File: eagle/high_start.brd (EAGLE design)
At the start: 100.8 x 80.8 mm, 34 parts, among them IC1 7805TV, Q1 16Mhz, Q2 IRF510, Q3 IRF510, Q4 IRF510, U2 ATMEGA328P_PDIP

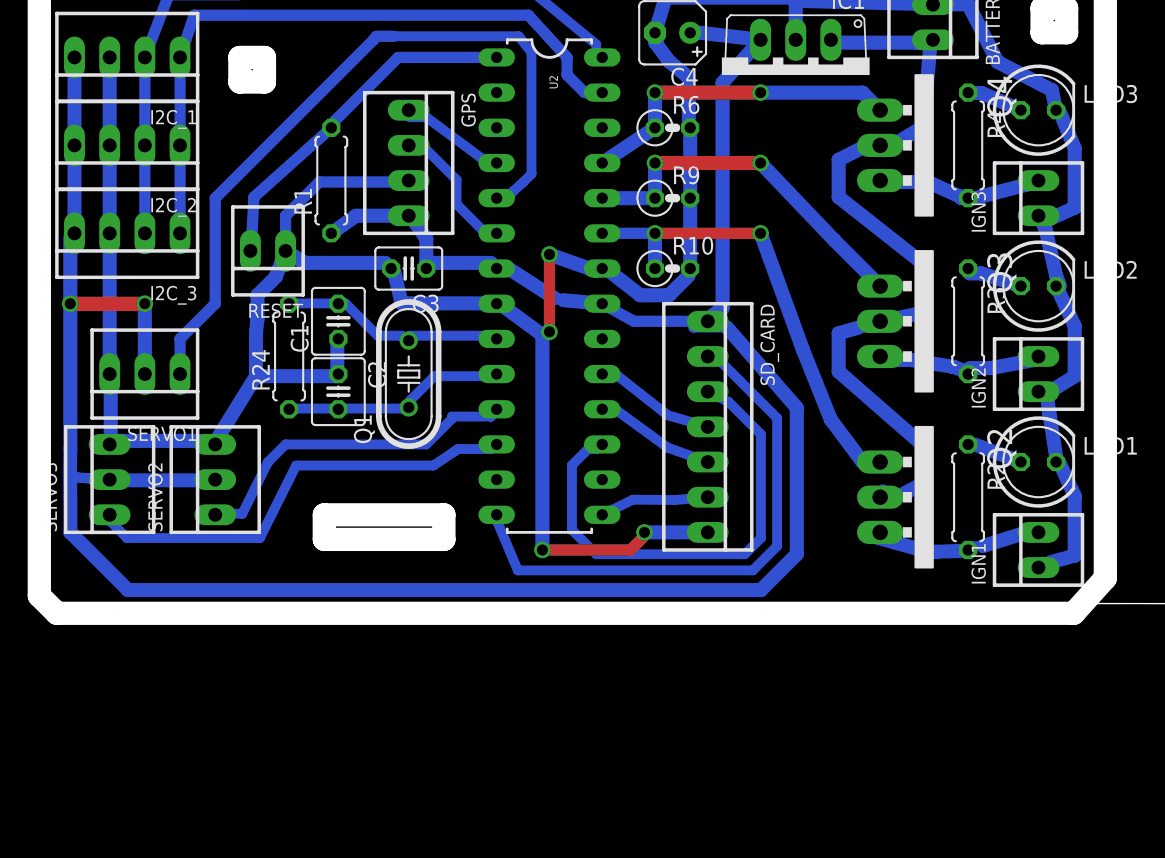
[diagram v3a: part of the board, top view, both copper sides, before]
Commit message: moved igniter FETs to low side
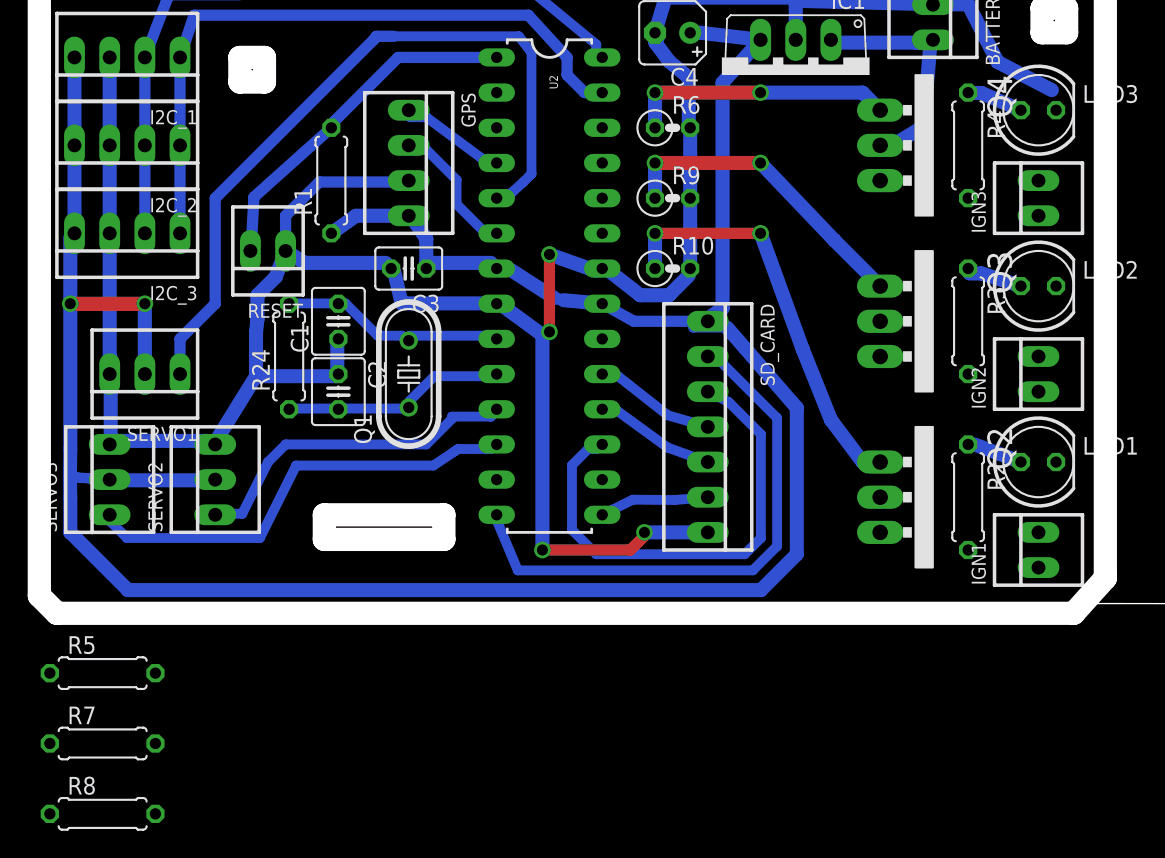
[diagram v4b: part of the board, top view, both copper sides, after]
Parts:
- added R5, R7, R8: 220, rcl:0207/7
- R2, R3, R4: value 330 -> 1k
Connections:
- new net N$12: IGN1.1, Q2.2, R2.2
- new net N$13: IGN2.1, Q3.2, R3.2
- new net N$14: IGN3.1, Q4.2, R4.2
- net +9V: now also IGN1.2, IGN2.2, IGN3.2; no longer Q2.2, Q3.2, Q4.2
- net GND: now also Q2.3, Q3.3, Q4.3; no longer IGN1.1, IGN2.1, IGN3.1
- net N$18: now also R5.2; no longer U2.23
- net N$19: now also R8.2; no longer U2.24
- net N$20: now also R7.2; no longer U2.25
- net N$24: now also R5.1, U2.23; no longer IGN1.2, Q2.3, R2.2
- net N$25: now also R7.1, U2.25; no longer IGN2.2, Q3.3, R3.2
- net N$26: now also R8.1, U2.24; no longer IGN3.2, Q4.3, R4.2
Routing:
- net GND: track 239.5 -> 197.1 mm
- net +9V: track 59.4 -> 18.0 mm
- net N$24: track 12.9 -> 0.00 mm
- net N$25: track 12.3 -> 0.00 mm
- net N$26: track 12.1 -> 0.00 mm
- net N$20: track 23.9 -> 19.3 mm
- net N$18: track 33.4 -> 29.6 mm
- net N$19: track 26.4 -> 22.6 mm

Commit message: janky rerouted
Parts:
- R10, R6, R9: device rcl:0207/2V -> rcl:0207/7
- moved R7 63.8 mm to (48.3, 35.6)
- moved R8 63.8 mm to (48.3, 30.5)
- moved R5 53.9 mm to (48.3, 25.4)
- moved R10 5.48 mm to (50.3, 22.9), turned to 180 degrees
- moved R9 5.48 mm to (50.3, 27.9), turned to 180 degrees
- moved R6 5.48 mm to (50.3, 33.0), turned to 180 degrees
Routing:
- net GND: track 197.1 -> 299.4 mm
- net +9V: track 18.0 -> 82.1 mm
- net N$14: track 0.00 -> 13.5 mm
- net N$13: track 0.00 -> 13.5 mm
- net N$12: track 0.00 -> 13.5 mm
- net N$19: track 22.6 -> 11.0 mm, vias 2 -> 0
- net N$18: track 29.6 -> 18.5 mm, vias 2 -> 0
- net N$20: track 19.3 -> 9.86 mm, vias 2 -> 0
- net N$25: track 0.00 -> 6.15 mm
- net N$26: track 0.00 -> 5.10 mm
- net N$24: track 0.00 -> 4.75 mm
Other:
- outline, holes or cut-outs redrawn

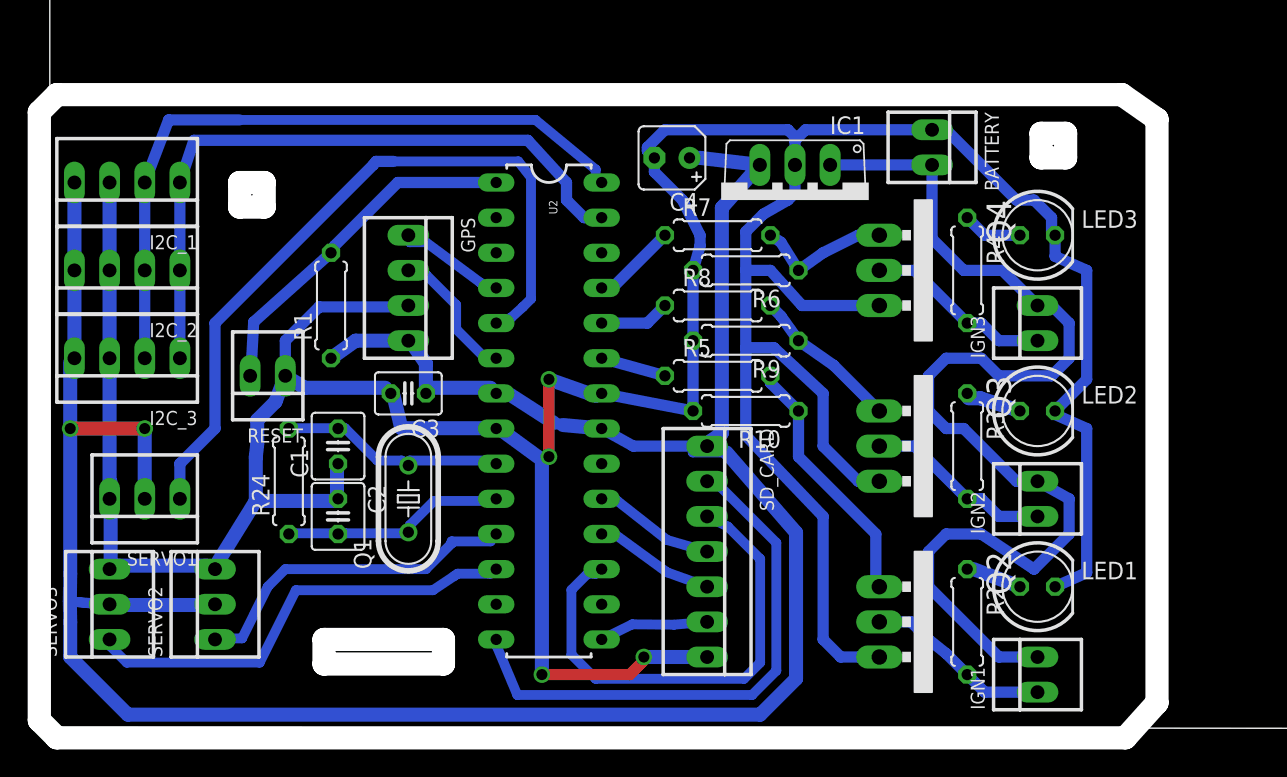
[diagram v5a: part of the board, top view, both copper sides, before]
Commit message: improved reroute
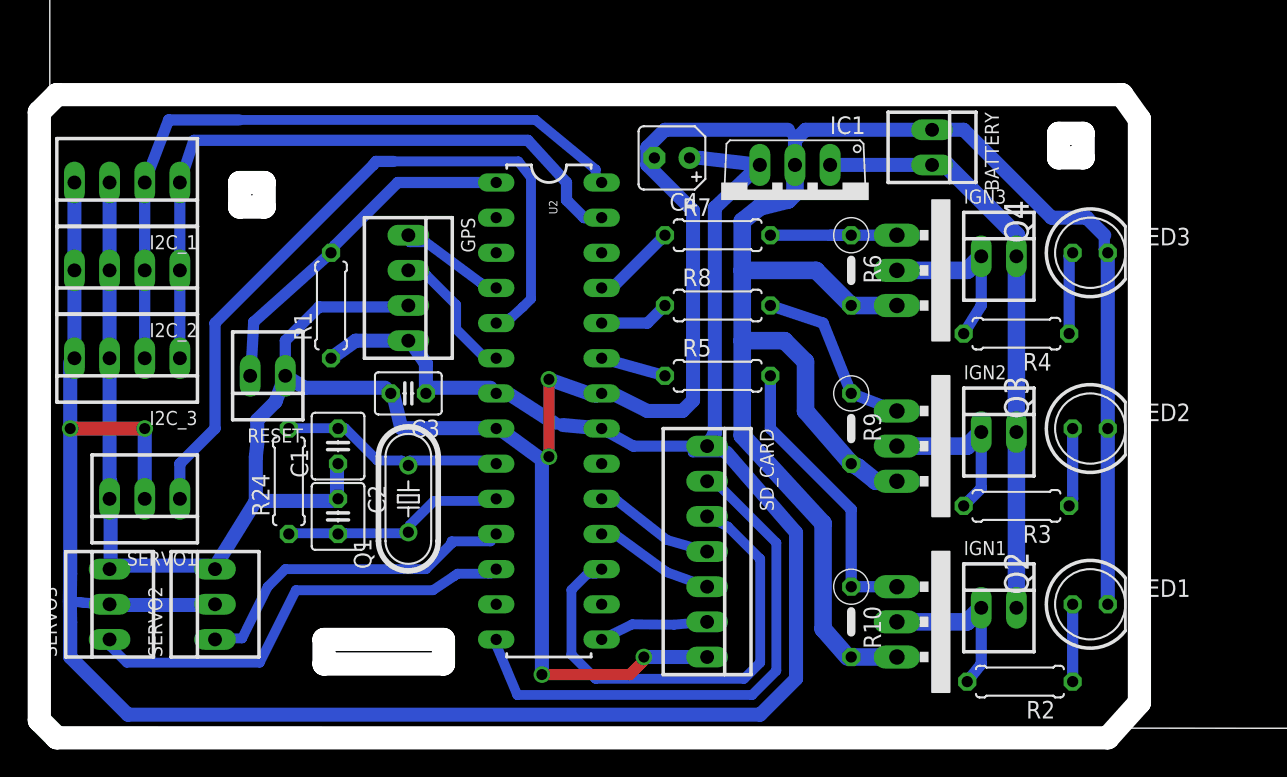
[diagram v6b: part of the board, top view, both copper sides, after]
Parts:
- R10, R6, R9: device rcl:0207/7 -> rcl:0207/5V
- moved R10 17.0 mm to (57.9, 7.62), turned to 270 degrees
- moved R9 9.92 mm to (57.9, 21.6), turned to 270 degrees
- moved R6 7.62 mm to (57.9, 33.0), turned to 270 degrees
- moved R4 5.79 mm to (69.8, 28.4), turned to 180 degrees
- moved R2 5.76 mm to (70.1, 3.30), turned to 180 degrees
- moved R3 5.59 mm to (69.8, 16.0), turned to 180 degrees
- moved IGN3 5.58 mm to (68.6, 34.0), turned to 0 degrees
- moved IGN1 5.58 mm to (68.6, 8.64), turned to 0 degrees
- moved IGN2 5.58 mm to (68.6, 21.3), turned to 0 degrees
- moved LED3 4.02 mm to (75.2, 34.3)
- moved LED1 4.02 mm to (75.2, 8.89)
- moved LED2 4.02 mm to (75.2, 21.6)
- moved Q2 1.27 mm to (67.6, 7.62)
- moved Q3 1.27 mm to (67.6, 20.3)
- moved Q4 1.27 mm to (67.6, 33.0)
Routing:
- net +9V: track 82.1 -> 42.5 mm
- net GND: track 299.4 -> 304.5 mm
- net N$18: track 18.5 -> 21.0 mm
- net N$19: track 11.0 -> 13.0 mm
- net N$23: track 4.34 -> 5.95 mm
- net N$22: track 4.22 -> 5.65 mm
- net N$21: track 4.30 -> 5.59 mm
- net N$12: track 13.5 -> 12.2 mm
- net N$13: track 13.5 -> 12.4 mm
- net N$14: track 13.5 -> 12.5 mm
- net N$20: track 9.86 -> 10.7 mm
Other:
- outline, holes or cut-outs redrawn
